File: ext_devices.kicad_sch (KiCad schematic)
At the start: 24 parts, among them CON1 MIKROBUS_HOST_CONN, J14 Conn_01x08_Female, J15 Conn_01x08_Female, U12 TXS0102DCU, U13 TXS0102DCU, U16 SN74LV1T34DBV, U17 SN74LV1T34DBV, U18 SN74LV1T34DBV, U19 SN74LV1T34DBV, U20 SN74LV1T34DBV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

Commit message: added SMD buzzer with several 3dmodels; rotated and moved ext pwr connector such that wires would go through a top plate opening
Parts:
- C148, C149, C150, C151, C152, C153: LCSC C49678 -> C307331
- U16, U17, U18, U19, U20, U21: LCSC (none) -> C100024
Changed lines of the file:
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@@
       (effects (font (size 1.27 1.27)) hide)
     )
-    (property "Datasheet" "https://datasheet.lcsc.com/lcsc/1810101813_YAGEO-CC0805KRX7R9BB104_C49678.pdf" (id 3) (at 262.89 110.49 0)
-      (effects (font (size 1.27 1.27)) hide)
-    )
-    (property "LCSC" "C49678" (id 4) (at 262.89 110.49 0)
+    (property "Datasheet" "https://datasheet.lcsc.com/lcsc/1810191222_Samsung-Electro-Mechanics-CL05B104KB54PNC_C307331.pdf" (id 3) (at 262.89 110.49 0)
+      (effects (font (size 1.27 1.27)) hide)
+    )
+    (property "LCSC" "C307331" (id 4) (at 262.89 110.49 0)
       (effects (font (size 1.27 1.27)) hide)
     )
@@
       (effects (font (size 1.27 1.27)) hide)
     )
+    (property "LCSC" "C100024" (id 4) (at 257.81 137.16 0)
+      (effects (font (size 1.27 1.27)) hide)
+    )
     (pin "1")
     (pin "2")
@@
       (effects (font (size 1.27 1.27)) hide)
     )
-    (property "Datasheet" "https://datasheet.lcsc.com/lcsc/1810101813_YAGEO-CC0805KRX7R9BB104_C49678.pdf" (id 3) (at 204.47 133.35 0)
-      (effects (font (size 1.27 1.27)) hide)
-    )
-    (property "LCSC" "C49678" (id 4) (at 204.47 133.35 0)
+    (property "Datasheet" "https://datasheet.lcsc.com/lcsc/1810191222_Samsung-Electro-Mechanics-CL05B104KB54PNC_C307331.pdf" (id 3) (at 204.47 133.35 0)
+      (effects (font (size 1.27 1.27)) hide)
+    )
+    (property "LCSC" "C307331" (id 4) (at 204.47 133.35 0)
       (effects (font (size 1.27 1.27)) hide)
     )
@@
       (effects (font (size 1.27 1.27)) hide)
     )
-    (property "Datasheet" "https://datasheet.lcsc.com/lcsc/1810101813_YAGEO-CC0805KRX7R9BB104_C49678.pdf" (id 3) (at 205.74 154.94 0)
-      (effects (font (size 1.27 1.27)) hide)
-    )
-    (property "LCSC" "C49678" (id 4) (at 205.74 154.94 0)
+    (property "Datasheet" "https://datasheet.lcsc.com/lcsc/1810191222_Samsung-Electro-Mechanics-CL05B104KB54PNC_C307331.pdf" (id 3) (at 205.74 154.94 0)
+      (effects (font (size 1.27 1.27)) hide)
+    )
+    (property "LCSC" "C307331" (id 4) (at 205.74 154.94 0)
       (effects (font (size 1.27 1.27)) hide)
     )
@@
       (effects (font (size 1.27 1.27)) hide)
     )
+    (property "LCSC" "C100024" (id 4) (at 257.81 120.65 0)
+      (effects (font (size 1.27 1.27)) hide)
+    )
     (pin "1")
     (pin "2")
@@
       (effects (font (size 1.27 1.27)) hide)
     )
+    (property "LCSC" "C100024" (id 4) (at 212.09 125.73 0)
+      (effects (font (size 1.27 1.27)) hide)
+    )
     (pin "1")
     (pin "2")
@@
       (effects (font (size 1.27 1.27)) hide)
     )
+    (property "LCSC" "C100024" (id 4) (at 212.09 146.05 0)
+      (effects (font (size 1.27 1.27)) hide)
+    )
     (pin "1")
     (pin "2")
@@
       (effects (font (size 1.27 1.27)) hide)
     )
+    (property "LCSC" "C100024" (id 4) (at 172.72 134.62 0)
+      (effects (font (size 1.27 1.27)) hide)
+    )
     (pin "1")
     (pin "2")
@@
       (effects (font (size 1.27 1.27)) hide)
     )
-    (property "Datasheet" "https://datasheet.lcsc.com/lcsc/1810101813_YAGEO-CC0805KRX7R9BB104_C49678.pdf" (id 3) (at 262.89 147.32 0)
-      (effects (font (size 1.27 1.27)) hide)
-    )
-    (property "LCSC" "C49678" (id 4) (at 262.89 147.32 0)
+    (property "Datasheet" "https://datasheet.lcsc.com/lcsc/1810191222_Samsung-Electro-Mechanics-CL05B104KB54PNC_C307331.pdf" (id 3) (at 262.89 147.32 0)
+      (effects (font (size 1.27 1.27)) hide)
+    )
+    (property "LCSC" "C307331" (id 4) (at 262.89 147.32 0)
       (effects (font (size 1.27 1.27)) hide)
     )
@@
       (effects (font (size 1.27 1.27)) hide)
     )
-    (property "Datasheet" "https://datasheet.lcsc.com/lcsc/1810101813_YAGEO-CC0805KRX7R9BB104_C49678.pdf" (id 3) (at 177.8 107.95 0)
-      (effects (font (size 1.27 1.27)) hide)
-    )
-    (property "LCSC" "C49678" (id 4) (at 177.8 107.95 0)
+    (property "Datasheet" "https://datasheet.lcsc.com/lcsc/1810191222_Samsung-Electro-Mechanics-CL05B104KB54PNC_C307331.pdf" (id 3) (at 177.8 107.95 0)
+      (effects (font (size 1.27 1.27)) hide)
+    )
+    (property "LCSC" "C307331" (id 4) (at 177.8 107.95 0)
       (effects (font (size 1.27 1.27)) hide)
     )
@@
       (effects (font (size 1.27 1.27)) hide)
     )
-    (property "Datasheet" "https://datasheet.lcsc.com/lcsc/1810101813_YAGEO-CC0805KRX7R9BB104_C49678.pdf" (id 3) (at 179.07 144.78 0)
-      (effects (font (size 1.27 1.27)) hide)
-    )
-    (property "LCSC" "C49678" (id 4) (at 179.07 144.78 0)
+    (property "Datasheet" "https://datasheet.lcsc.com/lcsc/1810191222_Samsung-Electro-Mechanics-CL05B104KB54PNC_C307331.pdf" (id 3) (at 179.07 144.78 0)
+      (effects (font (size 1.27 1.27)) hide)
+    )
+    (property "LCSC" "C307331" (id 4) (at 179.07 144.78 0)
       (effects (font (size 1.27 1.27)) hide)
     )
@@
       (effects (font (size 1.27 1.27)) hide)
     )
+    (property "LCSC" "C100024" (id 4) (at 172.72 118.11 0)
+      (effects (font (size 1.27 1.27)) hide)
+    )

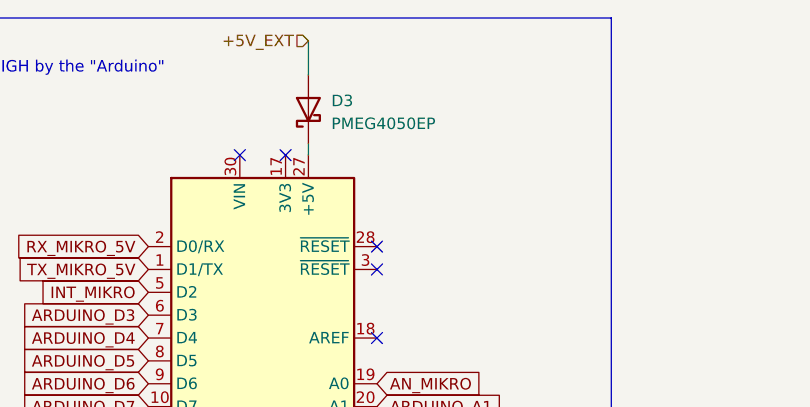
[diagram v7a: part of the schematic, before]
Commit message: updated arduino diode with the one that is in jlcpcb stock
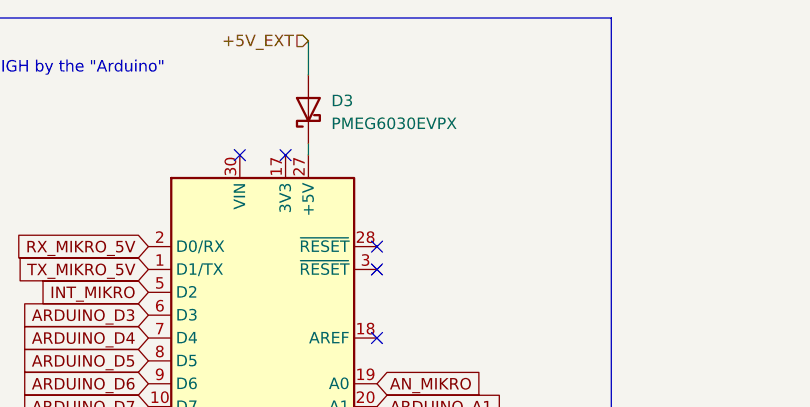
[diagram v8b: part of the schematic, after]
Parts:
- D3: value PMEG4050EP -> PMEG6030EVPX; LCSC C96235 -> C489223
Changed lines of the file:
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@@
       (effects (font (size 1.27 1.27)) (justify right))
     )
-    (property "Value" "PMEG4050EP" (id 1) (at 194.945 38.4174 90)
+    (property "Value" "PMEG6030EVPX" (id 1) (at 194.945 38.4174 90)
       (effects (font (size 1.27 1.27)) (justify right))
     )
@@
       (effects (font (size 1.27 1.27)) hide)
     )
-    (property "Datasheet" "https://datasheet.lcsc.com/lcsc/1811061814_Nexperia-PMEG4050EP-115_C96235.pdf" (id 3) (at 192.405 36.83 0)
+    (property "Datasheet" "https://datasheet.lcsc.com/lcsc/2201242200_Nexperia-PMEG6030EVPX_C489223.pdf" (id 3) (at 192.405 36.83 0)
       (effects (font (size 1.27 1.27)) hide)
     )
-    (property "LCSC" "C96235" (id 4) (at 192.405 36.83 0)
+    (property "LCSC" "C489223" (id 4) (at 192.405 36.83 0)
       (effects (font (size 1.27 1.27)) hide)
     )
